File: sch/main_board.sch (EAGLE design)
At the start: 16 parts, among them IC1 MCP73831T-2ACI_OT

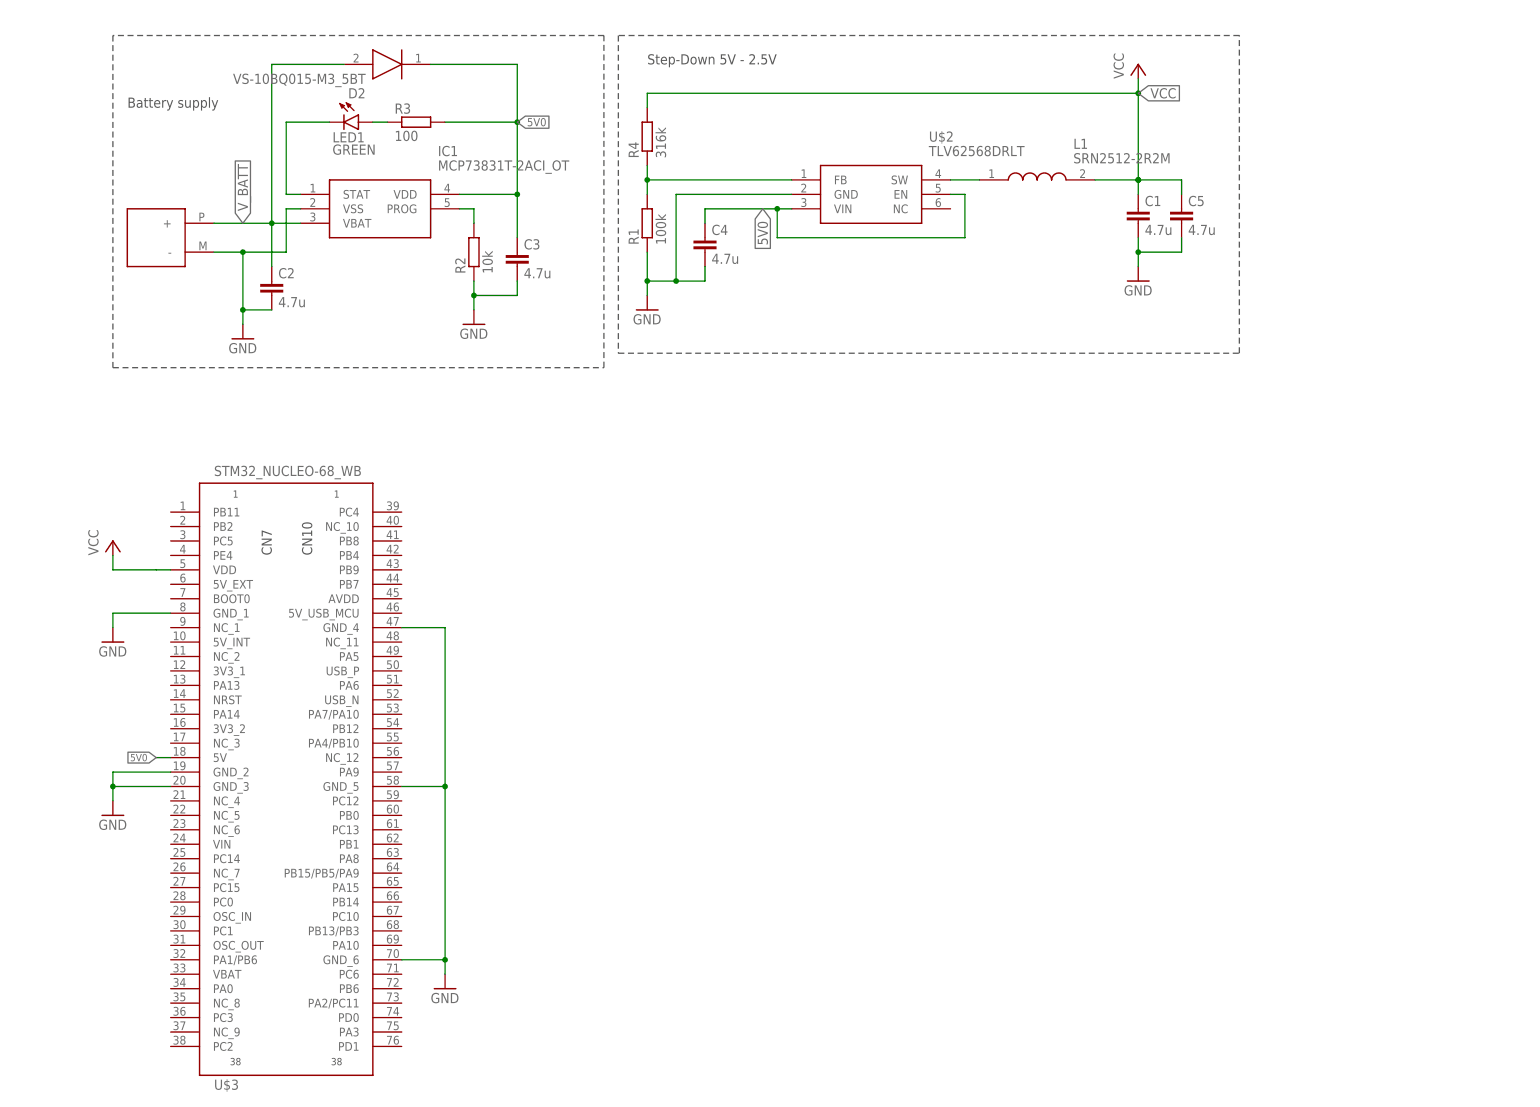
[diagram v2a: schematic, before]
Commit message: Add STM32WB board part, add sensor connector part
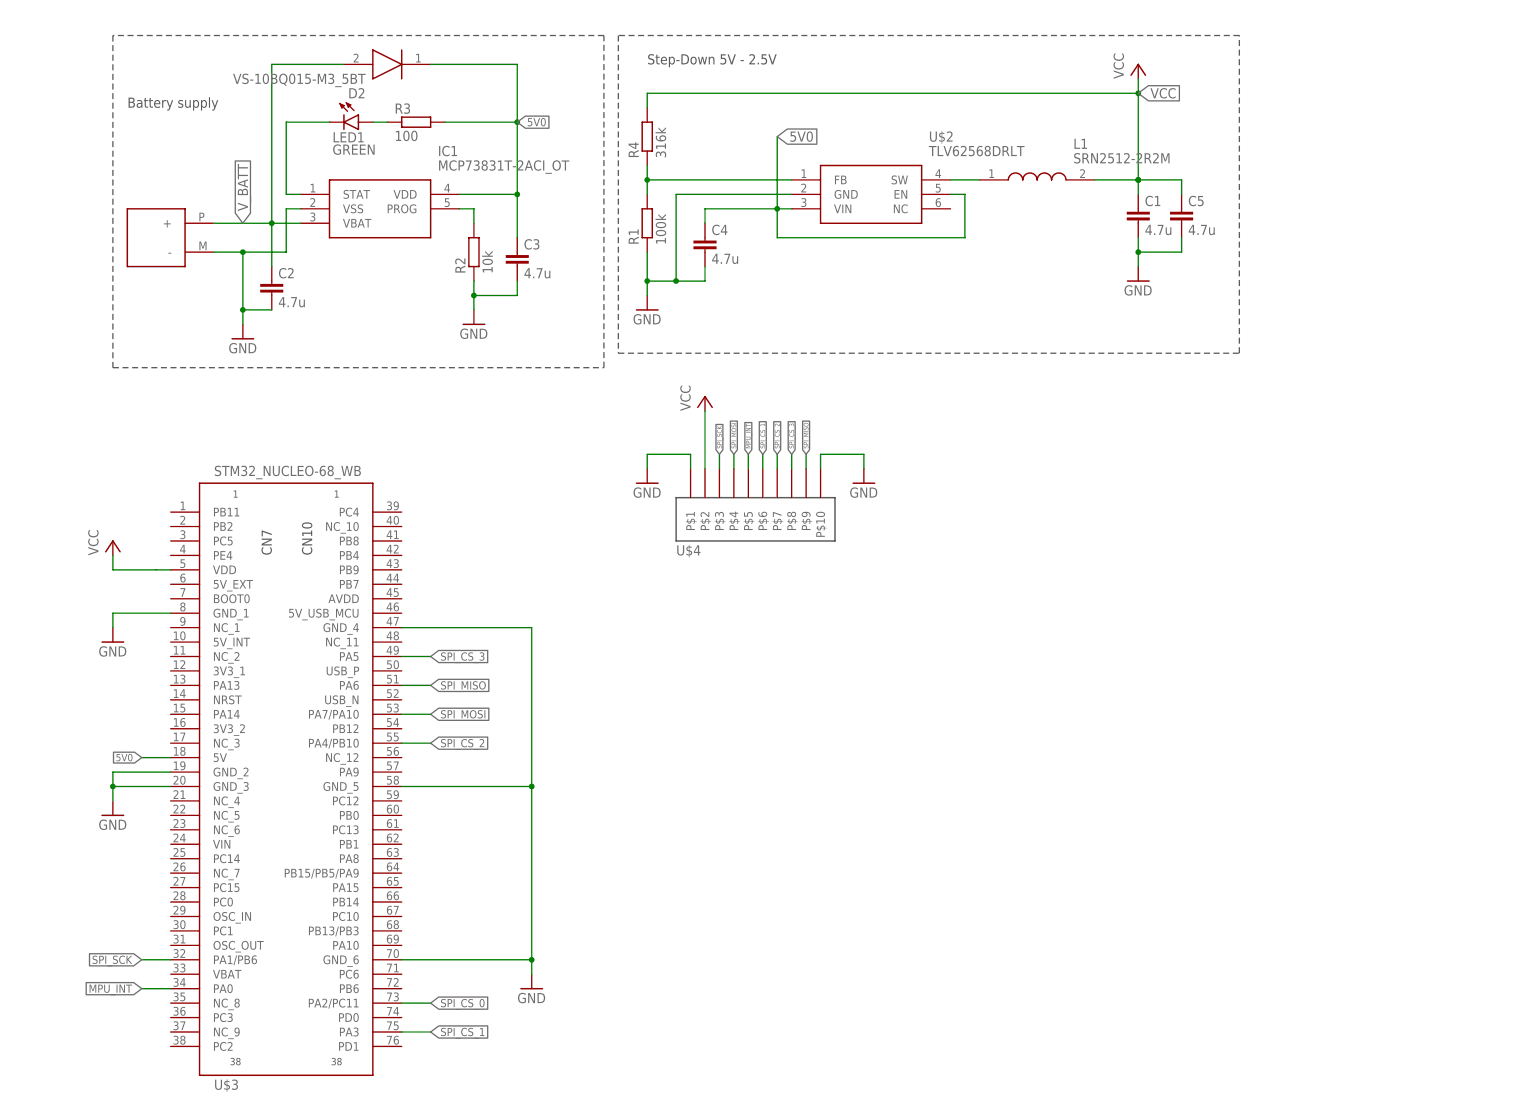
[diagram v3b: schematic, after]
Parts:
- added U$4: (no value), SamacSys_Parts:1-2178711-2
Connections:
- new net MPU_INT: U$3.PA0, U$4.P$5
- new net SPI_CS_0: U$3.PA2/PC11
- new net SPI_CS_1: U$3.PA3, U$4.P$6
- new net SPI_CS_2: U$3.PA4/PB10, U$4.P$7
- new net SPI_CS_3: U$3.PA5, U$4.P$8
- new net SPI_MISO: U$3.PA6, U$4.P$9
- new net SPI_MOSI: U$3.PA7/PA10, U$4.P$4
- new net SPI_SCK: U$3.PA1/PB6, U$4.P$3
- net GND: now also U$4.P$1, U$4.P$10
- net VCC: now also U$4.P$2
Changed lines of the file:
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@@
 <setting verticaltext="up"/>
 </settings>
-<grid distance="0.1" unitdist="inch" unit="inch" style="lines" multiple="1" display="no" altdistance="0.01" altunitdist="inch" altunit="inch"/>
+<grid distance="0.1" unitdist="inch" unit="inch" style="dots" multiple="1" display="yes" altdistance="0.01" altunitdist="inch" altunit="inch"/>
 <layers>
 <layer number="1" name="Top" color="4" fill="1" visible="no" active="no"/>
@@
 <part name="GND7" library="supply1" library_urn="urn:adsk.eagle:library:371" deviceset="GND" device=""/>
 <part name="P+2" library="supply1" library_urn="urn:adsk.eagle:library:371" deviceset="VCC" device=""/>
+<part name="GND8" library="supply1" library_urn="urn:adsk.eagle:library:371" deviceset="GND" device=""/>
+<part name="GND9" library="supply1" library_urn="urn:adsk.eagle:library:371" deviceset="GND" device=""/>
+<part name="P+3" library="supply1" library_urn="urn:adsk.eagle:library:371" deviceset="VCC" device=""/>
+<part name="U$4" library="SamacSys_Parts" deviceset="1-2178711-2" device=""/>
 </parts>
 <sheets>
@@
 <attribute name="VALUE" x="-12.7" y="40.64" size="1.778" layer="96"/>
 </instance>
-<instance part="GND7" gate="1" x="48.26" y="12.7" smashed="yes">
-<attribute name="VALUE" x="45.72" y="10.16" size="1.778" layer="96"/>
+<instance part="GND7" gate="1" x="63.5" y="12.7" smashed="yes">
+<attribute name="VALUE" x="60.96" y="10.16" size="1.778" layer="96"/>
 </instance>
 <instance part="P+2" gate="VCC" x="-10.16" y="91.44" smashed="yes">
 <attribute name="VALUE" x="-12.7" y="88.9" size="1.778" layer="96" rot="R90"/>
+</instance>
+<instance part="GND8" gate="1" x="83.82" y="101.6" smashed="yes">
+<attribute name="VALUE" x="81.28" y="99.06" size="1.778" layer="96"/>
+</instance>
+<instance part="GND9" gate="1" x="121.92" y="101.6" smashed="yes">
+<attribute name="VALUE" x="119.38" y="99.06" size="1.778" layer="96"/>
+</instance>
+<instance part="P+3" gate="VCC" x="93.98" y="116.84" smashed="yes">
+<attribute name="VALUE" x="91.44" y="114.3" size="1.778" layer="96" rot="R90"/>
+</instance>
+<instance part="U$4" gate="G$1" x="102.87" y="94.996" smashed="yes">
+<attribute name="NAME" x="88.9" y="88.9" size="1.778" layer="95"/>
+<attribute name="VALUE" x="106.68" y="88.9" size="1.778" layer="96"/>
 </instance>
 </instances>
@@
 <segment>
 <pinref part="U$3" gate="G$1" pin="GND_4"/>
-<wire x1="40.64" y1="76.2" x2="48.26" y2="76.2" width="0.1524" layer="91"/>
+<wire x1="40.64" y1="76.2" x2="63.5" y2="76.2" width="0.1524" layer="91"/>
 <pinref part="U$3" gate="G$1" pin="GND_5"/>
-<wire x1="48.26" y1="76.2" x2="48.26" y2="48.26" width="0.1524" layer="91"/>
-<wire x1="48.26" y1="48.26" x2="40.64" y2="48.26" width="0.1524" layer="91"/>
+<wire x1="63.5" y1="76.2" x2="63.5" y2="48.26" width="0.1524" layer="91"/>
+<wire x1="63.5" y1="48.26" x2="40.64" y2="48.26" width="0.1524" layer="91"/>
 <pinref part="U$3" gate="G$1" pin="GND_6"/>
-<wire x1="48.26" y1="48.26" x2="48.26" y2="17.78" width="0.1524" layer="91"/>
-<wire x1="48.26" y1="17.78" x2="40.64" y2="17.78" width="0.1524" layer="91"/>
-<wire x1="48.26" y1="17.78" x2="48.26" y2="15.24" width="0.1524" layer="91"/>
-<junction x="48.26" y="48.26"/>
-<junction x="48.26" y="17.78"/>
+<wire x1="63.5" y1="48.26" x2="63.5" y2="17.78" width="0.1524" layer="91"/>
+<wire x1="63.5" y1="17.78" x2="40.64" y2="17.78" width="0.1524" layer="91"/>
+<wire x1="63.5" y1="17.78" x2="63.5" y2="15.24" width="0.1524" layer="91"/>
+<junction x="63.5" y="48.26"/>
+<junction x="63.5" y="17.78"/>
 <pinref part="GND7" gate="1" pin="GND"/>
+</segment>
+<segment>
+<wire x1="91.44" y1="104.14" x2="91.44" y2="106.68" width="0.1524" layer="91"/>
+<wire x1="91.44" y1="106.68" x2="83.82" y2="106.68" width="0.1524" layer="91"/>
+<wire x1="83.82" y1="106.68" x2="83.82" y2="104.14" width="0.1524" layer="91"/>
+<pinref part="GND8" gate="1" pin="GND"/>
+<pinref part="U$4" gate="G$1" pin="P$1"/>
+</segment>
+<segment>
+<pinref part="GND9" gate="1" pin="GND"/>
+<wire x1="121.92" y1="104.14" x2="121.92" y2="106.68" width="0.1524" layer="91"/>
+<pinref part="U$4" gate="G$1" pin="P$10"/>
+<wire x1="121.92" y1="106.68" x2="114.3" y2="106.68" width="0.1524" layer="91"/>
+<wire x1="114.3" y1="106.68" x2="114.3" y2="104.14" width="0.1524" layer="91"/>
 </segment>
 </net>
@@
 <segment>
 <pinref part="U$2" gate="G$1" pin="VIN"/>
-<label x="104.14" y="149.86" size="1.778" layer="95" rot="R270" xref="yes"/>
+<label x="106.68" y="162.56" size="1.778" layer="95" xref="yes"/>
 <wire x1="109.22" y1="149.86" x2="106.68" y2="149.86" width="0.1524" layer="91"/>
 <pinref part="C4" gate="G$1" pin="1"/>
@@
 <pinref part="U$2" gate="G$1" pin="EN"/>
 <wire x1="139.7" y1="152.4" x2="137.16" y2="152.4" width="0.1524" layer="91"/>
+<wire x1="106.68" y1="149.86" x2="106.68" y2="162.56" width="0.1524" layer="91"/>
 </segment>
 <segment>
 <pinref part="U$3" gate="G$1" pin="5V"/>
-<wire x1="0" y1="53.34" x2="-2.54" y2="53.34" width="0.1524" layer="91"/>
-<label x="-2.54" y="53.34" size="1.27" layer="95" rot="R180" xref="yes"/>
+<wire x1="0" y1="53.34" x2="-5.08" y2="53.34" width="0.1524" layer="91"/>
+<label x="-5.08" y="53.34" size="1.27" layer="95" rot="R180" xref="yes"/>
 </segment>
 </net>
@@
 <wire x1="-10.16" y1="86.36" x2="-10.16" y2="88.9" width="0.1524" layer="91"/>
 </segment>
-</net>
+<segment>
+<pinref part="P+3" gate="VCC" pin="VCC"/>
+<wire x1="93.98" y1="104.14" x2="93.98" y2="114.3" width="0.1524" layer="91"/>
+<pinref part="U$4" gate="G$1" pin="P$2"/>
+</segment>
+</net>
+<net name="SPI_SCK" class="0">
+<segment>
+<pinref part="U$3" gate="G$1" pin="PA1/PB6"/>
+<wire x1="0" y1="17.78" x2="-5.08" y2="17.78" width="0.1524" layer="91"/>
+<label x="-5.08" y="17.78" size="1.4224" layer="95" rot="R180" xref="yes"/>
+</segment>
+<segment>
+<wire x1="96.52" y1="104.14" x2="96.52" y2="106.68" width="0.1524" layer="91"/>
+<label x="96.52" y="106.68" size="0.8128" layer="95" rot="R90" xref="yes"/>
+<pinref part="U$4" gate="G$1" pin="P$3"/>
+</segment>
+</net>
+<net name="MPU_INT" class="0">
+<segment>
+<pinref part="U$3" gate="G$1" pin="PA0"/>
+<wire x1="0" y1="12.7" x2="-5.08" y2="12.7" width="0.1524" layer="91"/>
+<label x="-5.08" y="12.7" size="1.4224" layer="95" rot="R180" xref="yes"/>
+</segment>
+<segment>
+<wire x1="101.6" y1="104.14" x2="101.6" y2="106.68" width="0.1524" layer="91"/>
+<label x="101.6" y="106.68" size="0.8128" layer="95" rot="R90" xref="yes"/>
+<pinref part="U$4" gate="G$1" pin="P$5"/>
+</segment>
+</net>
+<net name="SPI_MISO" class="0">
+<segment>
+<pinref part="U$3" gate="G$1" pin="PA6"/>
+<wire x1="40.64" y1="66.04" x2="45.72" y2="66.04" width="0.1524" layer="91"/>
+<label x="45.72" y="66.04" size="1.4224" layer="95" xref="yes"/>
+</segment>
+<segment>
+<wire x1="111.76" y1="104.14" x2="111.76" y2="106.68" width="0.1524" layer="91"/>
+<label x="111.76" y="106.68" size="0.8128" layer="95" rot="R90" xref="yes"/>
+<pinref part="U$4" gate="G$1" pin="P$9"/>
+</segment>
+</net>
+<net name="SPI_MOSI" class="0">
+<segment>
+<pinref part="U$3" gate="G$1" pin="PA7/PA10"/>
+<wire x1="40.64" y1="60.96" x2="45.72" y2="60.96" width="0.1524" layer="91"/>
+<label x="45.72" y="60.96" size="1.4224" layer="95" xref="yes"/>
+</segment>
+<segment>
+<wire x1="99.06" y1="104.14" x2="99.06" y2="106.68" width="0.1524" layer="91"/>
+<label x="99.06" y="106.68" size="0.8128" layer="95" rot="R90" xref="yes"/>
+<pinref part="U$4" gate="G$1" pin="P$4"/>
+</segment>
+</net>
+<net name="SPI_CS_0" class="0">
+<segment>
+<pinref part="U$3" gate="G$1" pin="PA2/PC11"/>
+<wire x1="40.64" y1="10.16" x2="45.72" y2="10.16" width="0.1524" layer="91"/>
+<label x="45.72" y="10.16" size="1.4224" layer="95" xref="yes"/>
+</segment>
+</net>
+<net name="SPI_CS_1" class="0">
+<segment>
+<pinref part="U$3" gate="G$1" pin="PA3"/>
+<wire x1="40.64" y1="5.08" x2="45.72" y2="5.08" width="0.1524" layer="91"/>
+<label x="45.72" y="5.08" size="1.4224" layer="95" xref="yes"/>
+</segment>
+<segment>
+<pinref part="U$4" gate="G$1" pin="P$6"/>
+<wire x1="104.14" y1="104.14" x2="104.14" y2="106.68" width="0.1524" layer="91"/>
+<label x="104.14" y="106.68" size="0.8128" layer="95" rot="R90" xref="yes"/>
+</segment>
+</net>
+<net name="SPI_CS_2" class="0">
+<segment>
+<pinref part="U$3" gate="G$1" pin="PA4/PB10"/>
+<wire x1="40.64" y1="55.88" x2="45.72" y2="55.88" width="0.1524" layer="91"/>
+<label x="45.72" y="55.88" size="1.4224" layer="95" xref="yes"/>
+</segment>
+<segment>
+<pinref part="U$4" gate="G$1" pin="P$7"/>
+<wire x1="106.68" y1="104.14" x2="106.68" y2="106.68" width="0.1524" layer="91"/>
+<label x="106.68" y="106.68" size="0.8128" layer="95" rot="R90" xref="yes"/>
+</segment>
+</net>
+<net name="SPI_CS_3" class="0">
+<segment>
+<pinref part="U$3" gate="G$1" pin="PA5"/>
+<wire x1="40.64" y1="71.12" x2="45.72" y2="71.12" width="0.1524" layer="91"/>
+<label x="45.72" y="71.12" size="1.4224" layer="95" xref="yes"/>
+</segment>
+<segment>
+<pinref part="U$4" gate="G$1" pin="P$8"/>
+<wire x1="109.22" y1="104.14" x2="109.22" y2="106.68" width="0.1524" layer="91"/>
+<label x="109.22" y="106.68" size="0.8128" layer="95" rot="R90" xref="yes"/>
+</segment>
+</net>

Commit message: Main board ver. 1.0
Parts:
- added JP1, JP2: (no value), pinhead-2:PINHD-1X04_2.54-SMD
- added R5: 10k, resistor:R-EU_R1206
- added S1: (no value), switch:255SB
- added U$5: (no value), SamacSys_Parts:74AHC126D,118
- R4: value 316k -> 402k
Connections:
- new net AD0/SDO: JP2.2, U$4.P$6, U$5.4A
- new net BUFFER_EN: R5.1, U$3.PC0, U$5.1OE, U$5.2OE, U$5.4OE
- new net N$4: S1.O, U$1.+
- new net SCL/SCLK: JP1.1, U$4.P$3, U$5.1Y
- new net SDA/SDI: JP1.2, U$4.P$4, U$5.2Y
- net GND: now also JP1.4, U$5.3OE, U$5.GND
- net MPU_INT: now also JP2.4; no longer U$4.P$5
- net SPI_CS_0: now also JP2.3
- net SPI_CS_1: now also U$4.P$7; no longer U$4.P$6
- net SPI_CS_2: now also U$4.P$8; no longer U$4.P$7
- net SPI_CS_3: now also U$4.P$9; no longer U$4.P$8
- net SPI_MISO: now also U$5.4Y; no longer U$4.P$9
- net SPI_MOSI: now also U$5.2A; no longer U$4.P$4
- net SPI_SCK: now also U$5.1A; no longer U$4.P$3
- net VCC: now also JP1.3, R5.2, U$4.P$5, U$5.VCC
- net V_BATT: now also S1.P; no longer U$1.+
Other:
- note added: "MPU-9250"
- note added: "Step-Down 5V - 3V"
- note removed: "Step-Down 5V - 2.5V"
- moved on the sheet: U$3, U$4
